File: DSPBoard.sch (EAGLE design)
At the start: 429 parts, among them IC1 AD1939WBSTZ, IC10 LM833D, IC11 LM833D, IC12 TL074D, IC2 24AA1025, IC29 TL074D, IC3 LM4040B10DBZ, IC4 LM833D, IC5 LM833D, IC6 LM833D, IC7 LM833D, IC8 LM833D, IC9 LM833D, U1 LM11173.3NOPB, U2 PEC11R-4315F-N0012, U3 PEC11R-4315F-N0012, X1 2510-, Y1 12.288MHz

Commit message: started laying out the psu
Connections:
- net GND: now also SV1.3, SV1.4, SV1.7, SV1.8
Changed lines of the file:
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@@
 <pinref part="GND9" gate="1" pin="GND"/>
 <wire x1="22.86" y1="165.1" x2="20.32" y2="165.1" width="0.1524" layer="91"/>
+<pinref part="SV1" gate="G$1" pin="4"/>
+<wire x1="22.86" y1="167.64" x2="20.32" y2="167.64" width="0.1524" layer="91"/>
+<wire x1="20.32" y1="167.64" x2="20.32" y2="165.1" width="0.1524" layer="91"/>
+<junction x="20.32" y="165.1"/>
+<pinref part="SV1" gate="G$1" pin="8"/>
+<wire x1="22.86" y1="162.56" x2="20.32" y2="162.56" width="0.1524" layer="91"/>
+<wire x1="20.32" y1="162.56" x2="20.32" y2="165.1" width="0.1524" layer="91"/>
 </segment>
 <segment>
@@
 <pinref part="GND8" gate="1" pin="GND"/>
 <wire x1="40.64" y1="165.1" x2="38.1" y2="165.1" width="0.1524" layer="91"/>
+<pinref part="SV1" gate="G$1" pin="7"/>
+<wire x1="38.1" y1="162.56" x2="40.64" y2="162.56" width="0.1524" layer="91"/>
+<wire x1="40.64" y1="162.56" x2="40.64" y2="165.1" width="0.1524" layer="91"/>
+<junction x="40.64" y="165.1"/>
+<pinref part="SV1" gate="G$1" pin="3"/>
+<wire x1="38.1" y1="167.64" x2="40.64" y2="167.64" width="0.1524" layer="91"/>
+<wire x1="40.64" y1="167.64" x2="40.64" y2="165.1" width="0.1524" layer="91"/>
 </segment>
 <segment>

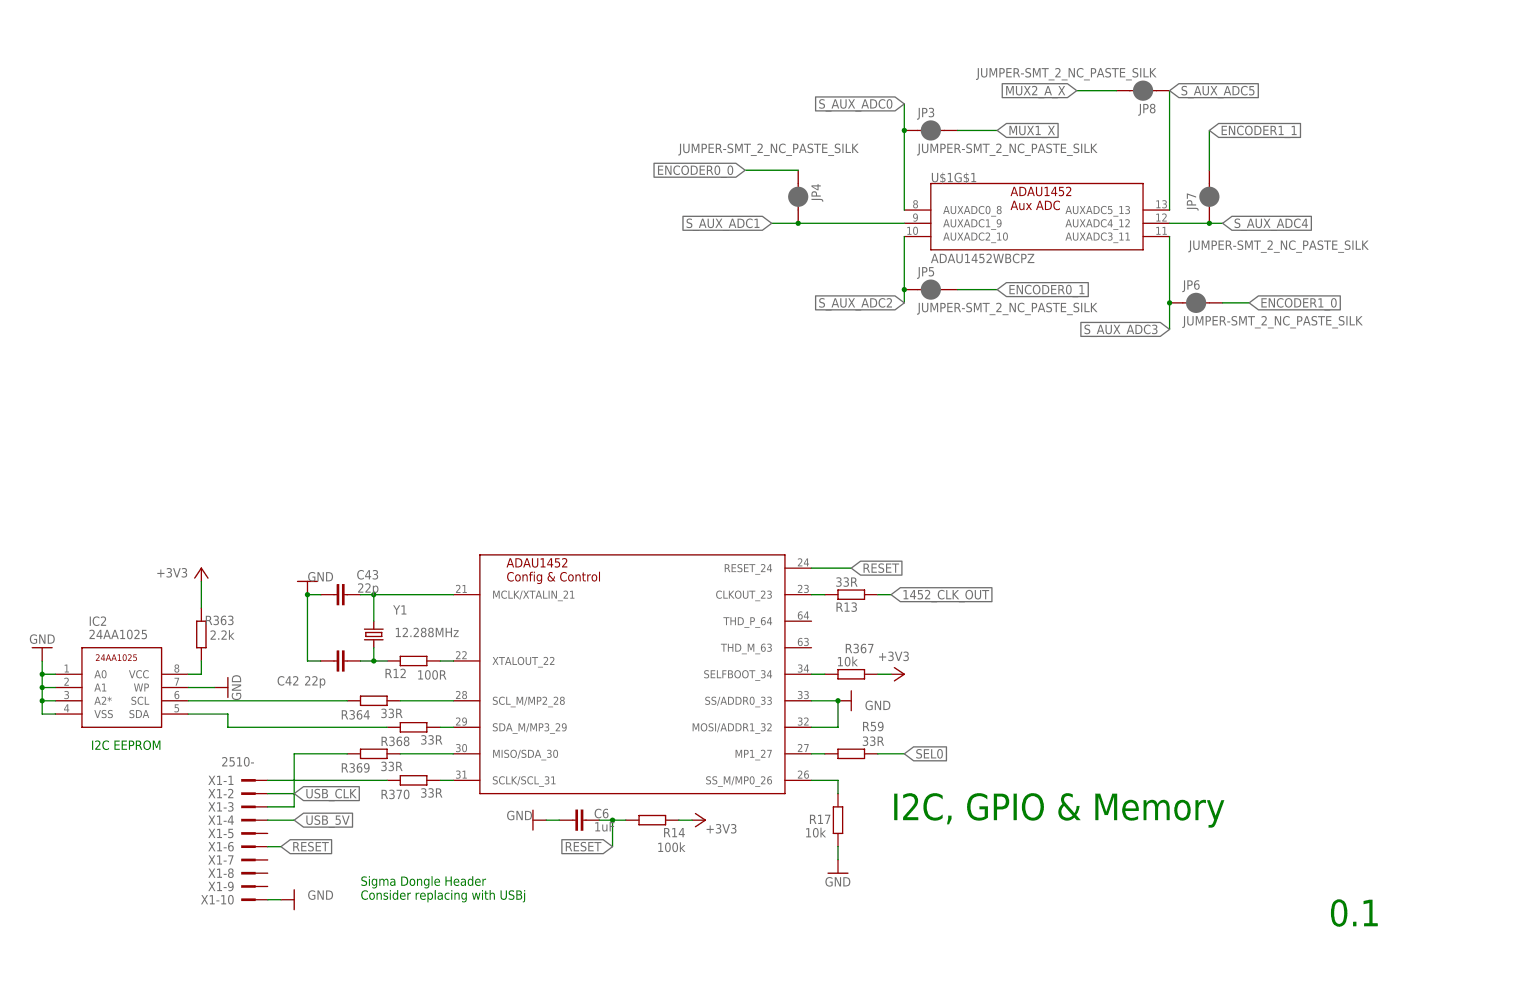
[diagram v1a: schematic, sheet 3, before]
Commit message: some layout changes, need to make daves recomended changes
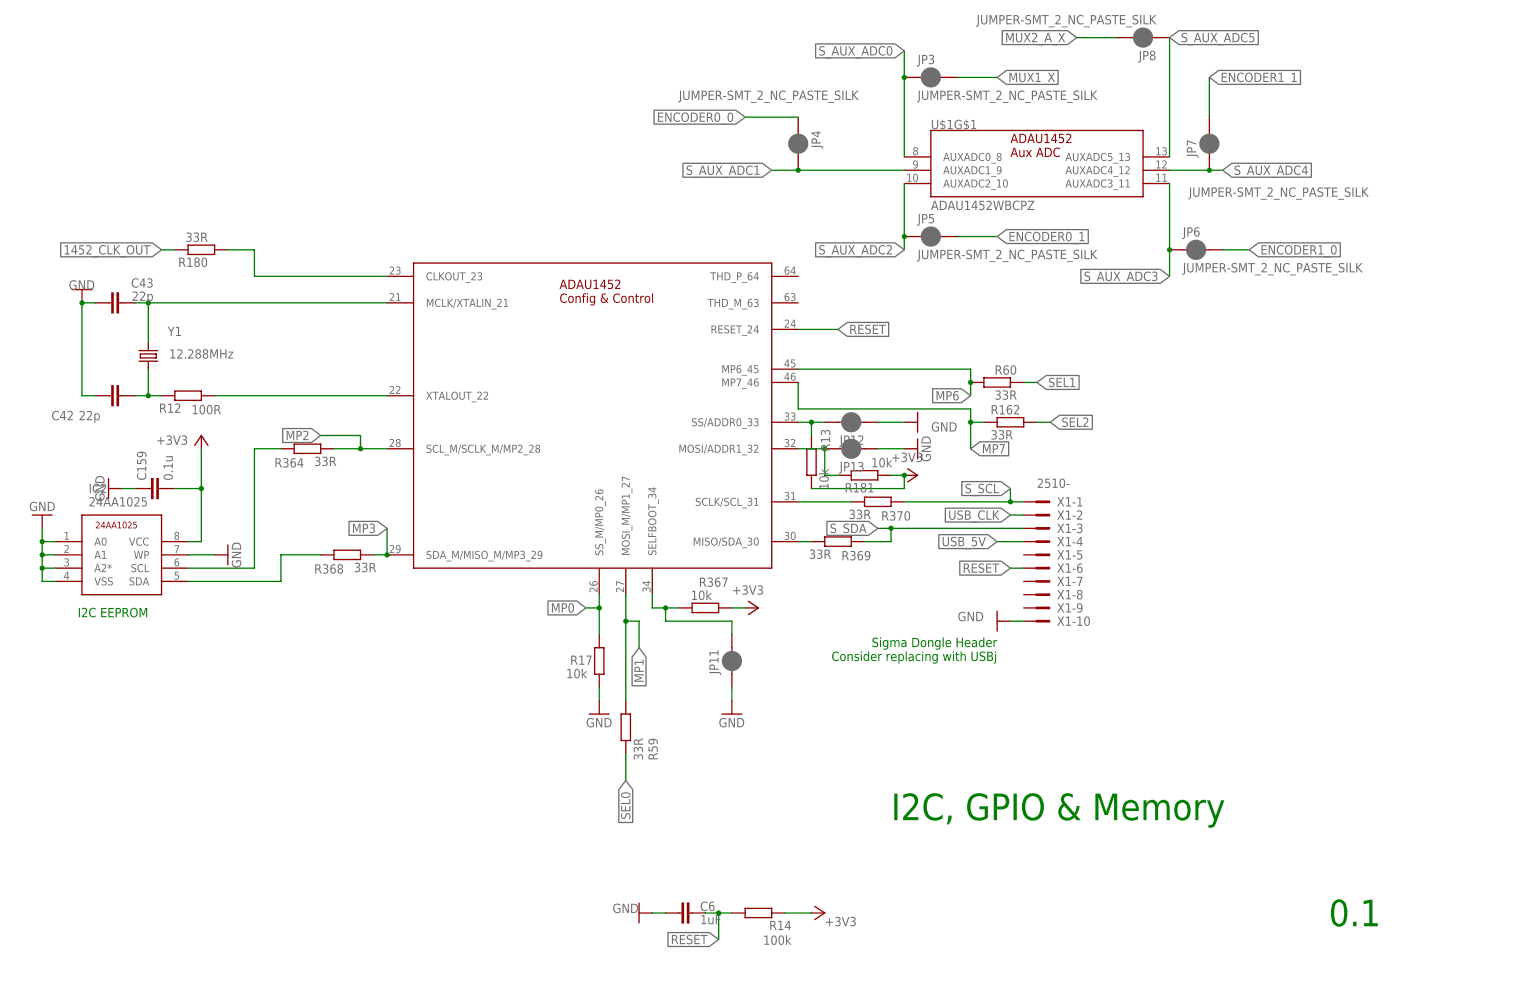
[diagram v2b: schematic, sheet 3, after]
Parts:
- removed R363: 2.2k, rcl:R-EU_R0603
- added C157, C158: 100nF, rcl:C-EUC0603
- added C159: 0.1u, rcl:C-EUC0603
- added JP11, JP12, JP13, JP14, JP15, JP16: JUMPER-SMT_2_NC_PASTE_SILK, SparkFun-Jumpers:JUMPER-SMT_2_NC_PASTE_SILK
- added R156, R157, R158, R159, R175, R176, R180: 33R, rcl:R-EU_R0603
- added R177: 240R, rcl:R-EU_R0603
- added R178: 100R, rcl:R-EU_R0603
- added R179: 75R, rcl:R-EU_R0603
- added R181: 10k, rcl:R-EU_R0603
- added SPDIF: (no value), con-lstb:MA04-1
- R13: value 33R -> 10k
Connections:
- removed net N$135: MUX2_RIPPLECOUNTERA.Q4, MUX2_RIPPLECOUNTERA.Q5, MUX2_RIPPLECOUNTERA.Q6, MUX2_RIPPLECOUNTERA.Q7, MUX2_RIPPLECOUNTERA.RES
- removed net N$162: R162.1, U$1G$5.MP7_46
- removed net N$546: R13.2, U$1G$2.CLKOUT_23
- removed net N$547: R364.1, U$1G$2.SCL_M/MP2_28
- removed net N$550: R368.1, U$1G$2.SDA_M/MP3_29
- removed net N$551: R60.2, U$1G$5.MP6_45
- removed net N$556: MUX1_RIPPLECOUNTERA.Q4, MUX1_RIPPLECOUNTERA.Q5, MUX1_RIPPLECOUNTERA.Q6, MUX1_RIPPLECOUNTERA.Q7, MUX1_RIPPLECOUNTERA.RES
- removed net N$7: IC2.VCC, R363.1
- removed net S_MP0: R174.2
- removed net S_MP1: R173.2
- removed net S_MP10: R164.2
- removed net S_MP11: R163.2
- removed net S_MP12: R161.2
- removed net S_MP13: R160.2
- removed net S_MP2: R172.2
- removed net S_MP3: R171.2
- removed net S_MP4: R170.2
- removed net S_MP5: R169.2
- removed net S_MP6: R168.2
- removed net S_MP7: R167.2
- removed net S_MP8: R166.2
- removed net S_MP9: R165.2
- new net DSP_47: JP15.1, R24.1, U$1G$5.LRCLK_OUT2/MP8_47
- new net DSP_50: JP16.1, R56.1, U$1G$5.LRCLK_OUT3/MP9_50
- new net MP0: R17.1, R174.2, U$1G$2.SS_M/MP0_26
- new net MP1: R173.2, R59.1, U$1G$2.MOSI_M/MP1_27
- new net MP10: R164.2, R8.2, U$1G$4.LRCLK_IN0/MP10_58
- new net MP11: R163.2, R27.1, U$1G$4.LRCLK_IN1/MP11_61
- new net MP12: R156.1, R161.2, U$1G$4.LRCLK_IN2/MP12_66
- new net MP13: R157.1, R160.2, U$1G$4.LRCLK_IN3/MP13_69
- new net MP2: R172.2, R364.1, U$1G$2.SCL_M/SCLK_M/MP2_28
- new net MP3: R171.2, R368.1, U$1G$2.SDA_M/MISO_M/MP3_29
- new net MP4: JP14.1, JP14.2, R170.2, R18.2, U$1G$5.LRCLK_OUT0/MP4_39
- new net MP5: R142.2, R169.2, U$1G$5.LRCLK_OUT1/MP5_42
- new net MP6: R168.2, R60.2, U$1G$2.MP6_45
- new net MP7: R162.1, R167.2, U$1G$2.MP7_46
- new net MP8: JP15.2, R166.2
- new net MP9: JP16.2, R165.2
- new net N$142: JP12.2, R13.2, U$1G$2.SS/ADDR0_33
- new net N$157: JP13.2, R181.2, U$1G$2.MOSI/ADDR1_32
- net +3V3: now also C159.2, IC2.VCC, R13.1, R181.1; no longer R363.2
- net 1452_CLK_OUT: now also R180.2; no longer R13.1
- net GND: now also C159.1, JP11.1, JP12.1, JP13.1, R178.1, R179.2, SPDIF.2, SPDIF.3; no longer U$1G$2.MOSI/ADDR1_32, U$1G$2.SS/ADDR0_33
- net N$129: now also C158.2, R177.2; no longer R18.2, U$1G$5.LRCLK_OUT0/MP4_39
- net N$130: now also R158.1, U$1G$4.SDATA_IN3_70; no longer R142.2, U$1G$5.LRCLK_OUT1/MP5_42
- net N$138: now also R177.1, R178.2, SPDIF.1; no longer R27.1, U$1G$4.LRCLK_IN1/MP11_61
- net N$141: now also R180.1, U$1G$2.CLKOUT_23; no longer R24.1, U$1G$5.LRCLK_OUT2/MP8_47
- net N$30: now also R175.2, U$1G$4.BCLK_IN2_65; no longer R17.1, U$1G$2.SS_M/MP0_26
- net N$31: now also C157.1, U$1G$6.SPDIFIN_4; no longer R59.1, U$1G$2.MP1_27
- net N$32: now also C158.1, U$1G$6.SPDIFOUT_5; no longer R370.2, X1-1.KL
- net N$33: now also R159.1, U$1G$4.BCLK_IN3_68; no longer R8.2, U$1G$4.LRCLK_IN0/MP10_58
- net N$37: now also C157.2, R179.1, SPDIF.4; no longer R369.2, X1-3.KL
- net N$39: now also R176.2, U$1G$4.SDATA_IN2_67; no longer R56.1, U$1G$5.LRCLK_OUT3/MP9_50
- net N$545: now also JP11.2
- net SDATA_IN2_BCLK: now also R175.1
- net SDATA_IN2_DATA: now also R176.1
- net SDATA_IN2_LRCLK: now also R156.2
- net SDATA_IN3_BCLK: now also R159.2
- net SDATA_IN3_DATA: now also R158.2
- net SDATA_IN3_LRCLK: now also R157.2
- net SEL1: now also MUX1_RIPPLECOUNTERA.RES
- net SEL2: now also MUX2_RIPPLECOUNTERA.RES
- net S_SCL: now also R370.2, X1-1.KL
- net S_SDA: now also R369.2, X1-3.KL
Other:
- note added: "Check that 0.1 is enough"
- moved on the sheet: C1, C2, C3, C4, C40, C41, C42, C43, C5, C6, IC2, JP3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

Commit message: double-check and confirm opamp audio gains (not CV)
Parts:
- removed C133, C49, C58, C69: 10nF, rcl:C-EUC0603
- added C160: 10uF, rcl:C-EUC0603
- added C161: 0.1uF, rcl:C-EUC0603
- added CBST: 100nF, AcceleratedDesigns_Lib:C0603C104Z3VACTUC0603C104Z3VACTU
- added CIN: 22uF, AcceleratedDesigns_Lib:C2012X5R1V226M125ACC2012X5R1V226M125AC
- added COUT: 47uF, AcceleratedDesigns_Lib:C3216X5R1E476M160ACC3216X5R1E476M160AC
- added GND: WB_GND, AcceleratedDesigns_Lib:WB_GNDWB_GND
- added IOUT: WB_CURRENT_LOAD, AcceleratedDesigns_Lib:WB_CURRENT_LOADWB_CURRENT_LOAD
- added JP17, JP18, JP19, JP20: JUMPER-SMT_2_NC_PASTE_SILK, SparkFun-Jumpers:JUMPER-SMT_2_NC_PASTE_SILK
- added L1: 4.7uH, AcceleratedDesigns_Lib:CDPH4D19FNP-4R7MCCDPH4D19FNP-4R7MC
- added R182, R183, R184, R185: 100, rcl:R-EU_R0603
- added RFBB: 10k, AcceleratedDesigns_Lib:RC0201FR-0710KLRC0201FR-0710KL
- added RFBT: 61.9k, AcceleratedDesigns_Lib:CRCW040261K9FKEDCRCW040261K9FKED
- added SV2: (no value), con-lstb:MA04-1
- added U4: TPS561201DDCR, AcceleratedDesigns_Lib:TPS561201DDCRTPS561201DDCR
- added VIN: WB_BATTERY, AcceleratedDesigns_Lib:WB_BATTERYWB_BATTERY
- C119, C121: value 22uF -> 47uF; device rcl:C-EUC0603 -> rcl:CPOL-EUD
- C122: value 0.1u -> 390pF
- C123: value 0.1u -> 5.6nF
- C137: value 0.1uF -> 100uF
- C32: value 0.1uF -> 10uF
- R135: value 562 -> 562R
- R15, R31, R49, R65: value 15k -> 18k
- R364, R368, R369, R370: value 33R -> 2k2
- R39, R46, R62, R72: value 10k -> 6k2
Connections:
- removed net DSDATA3: IC1.DSDATA3
- removed net DSDATA4: IC1.DSDATA4
- removed net N$234: D1.3, D3.3, D5.3, D7.3
- removed net N$235: D2.3, D4.3, D6.3, D8.3
- removed net N$549: IC2.SCL, R364.2
- removed net N$552: IC2.SDA, R368.2
- removed net N$553: R370.1, U$1G$2.SCLK/SCL_31
- removed net N$554: R369.1, U$1G$2.MISO/SDA_30
- new net 0: CIN.2@2, COUT.2@2, GND.1@1, IOUT.-@2, RFBB.2@2, U4.GND@1, VIN.-@2
- new net 1: CIN.1@1, U4.EN@5, U4.VIN@3, VIN.+@1
- new net 2: CBST.1@1, L1.1@1, U4.SW@2
- new net 3: RFBB.1@1, RFBT.2@2, U4.VFB@4
- new net 4: COUT.1@1, IOUT.+@1, L1.2@2, RFBT.1@1
- new net 5: CBST.2@2, U4.VBST@6
- new net N$135: IC1.!CLATCH, JP20.1, SV2.1
- new net N$158: IC1.CCLK, JP19.1, SV2.2
- new net N$159: IC1.COUT, JP18.1, SV2.3
- new net N$160: R182.2, R39.1
- new net N$161: R185.2, R46.1
- new net N$162: R183.2, R62.1
- new net N$163: R184.2, R72.1
- new net N$7: IC1.CIN, JP17.1, SV2.4
- net +3V3: now also C160.2, C161.2, R364.2, R368.1, R369.1, R370.1
- net AIN0+: now also D2.3
- net AIN0-: now also D1.3
- net AIN1+: now also D4.3
- net AIN1-: now also D3.3
- net AIN2+: now also D7.3
- net AIN2-: now also D8.3
- net AIN3+: now also D6.3
- net AIN3-: now also D5.3
- net ASDATA2: no longer IC1.ASDATA2
- net DSDATA2: no longer IC1.DSDATA2
- net FILTR: now also C121.+; no longer C121.1
- net GND: now also C119.-, C121.-, C160.1, C161.1, JP17.2, JP18.2, JP19.2, JP20.2; no longer C119.2, C121.2, IC1.!CLATCH, IC1.CCLK, IC1.CIN, IC1.COUT
- net MP2: now also IC2.SCL
- net MP3: now also IC2.SDA, R368.2; no longer R368.1
- net N$10: no longer C49.1
- net N$18: now also R182.1; no longer R39.1
- net N$36: now also R185.1; no longer R46.1
- net N$38: no longer C58.2
- net N$40: no longer C58.1
- net N$47: now also R183.1; no longer R62.1
- net N$48: no longer C69.2
- net N$49: no longer C69.1
- net N$56: now also R184.1; no longer R72.1
- net N$57: no longer C133.2
- net N$58: no longer C133.1
- net N$75: now also C119.+; no longer C119.1
- net N$9: no longer C49.2
- net S_SCL: now also U$1G$2.SCLK/SCL_31
- net S_SDA: now also U$1G$2.MISO/SDA_30
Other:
- note removed: "Check that 0.1 is enough"

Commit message: Chekcing and some bug fixes complete, plus psu layout touchup
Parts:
- removed C156: 100n, rcl:C-EUC0603
- removed CBST: 100nF, AcceleratedDesigns_Lib:C0603C104Z3VACTUC0603C104Z3VACTU
- removed CIN: 22uF, AcceleratedDesigns_Lib:C2012X5R1V226M125ACC2012X5R1V226M125AC
- removed COUT: 47uF, AcceleratedDesigns_Lib:C3216X5R1E476M160ACC3216X5R1E476M160AC
- removed GND: WB_GND, AcceleratedDesigns_Lib:WB_GNDWB_GND
- removed IOUT: WB_CURRENT_LOAD, AcceleratedDesigns_Lib:WB_CURRENT_LOADWB_CURRENT_LOAD
- removed L1: 4.7uH, AcceleratedDesigns_Lib:CDPH4D19FNP-4R7MCCDPH4D19FNP-4R7MC
- removed MUX1_RIPPLECOUNTER, MUX2_RIPPLECOUNTER: 4024D, 40xx:4024D
- removed RFBB: 10k, AcceleratedDesigns_Lib:RC0201FR-0710KLRC0201FR-0710KL
- removed RFBT: 61.9k, AcceleratedDesigns_Lib:CRCW040261K9FKEDCRCW040261K9FKED
- removed U4: TPS561201DDCR, AcceleratedDesigns_Lib:TPS561201DDCRTPS561201DDCR
- removed VIN: WB_BATTERY, AcceleratedDesigns_Lib:WB_BATTERYWB_BATTERY
- added IC13: 4520D, 45xx:4520D
- C128, C129, C130, C131, C146, C147, C150, C151: value 0.1u -> 1n
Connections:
- removed net 0: CIN.2@2, COUT.2@2, GND.1@1, IOUT.-@2, RFBB.2@2, U4.GND@1, VIN.-@2
- removed net 1: CIN.1@1, U4.EN@5, U4.VIN@3, VIN.+@1
- removed net 2: CBST.1@1, L1.1@1, U4.SW@2
- removed net 3: RFBB.1@1, RFBT.2@2, U4.VFB@4
- removed net 4: COUT.1@1, IOUT.+@1, L1.2@2, RFBT.1@1
- removed net 5: CBST.2@2, U4.VBST@6
- net +5V: now also IC13P.VDD; no longer C156.1, MUX1_RIPPLECOUNTERP.VDD, MUX2_RIPPLECOUNTERP.VDD
- net GND: now also IC12B.+IN, IC12D.+IN, IC13P.VSS, IC29B.+IN, IC29D.+IN; no longer C156.2, IC12B.-IN, IC12D.-IN, IC29B.-IN, IC29D.-IN, MUX1_RIPPLECOUNTERP.VSS, MUX2_RIPPLECOUNTERP.VSS
- net MUX1_A: now also IC13A.Q0; no longer MUX1_RIPPLECOUNTERA.Q1
- net MUX1_B: now also IC13A.Q1; no longer MUX1_RIPPLECOUNTERA.Q2
- net MUX1_C: now also IC13A.Q2; no longer MUX1_RIPPLECOUNTERA.Q3
- net MUX2_A_A: now also IC13B.Q0; no longer MUX2_RIPPLECOUNTERA.Q1
- net MUX2_A_B: now also IC13B.Q1; no longer MUX2_RIPPLECOUNTERA.Q2
- net MUX2_A_C: now also IC13B.Q2; no longer MUX2_RIPPLECOUNTERA.Q3
- net N$116: now also IC12B.-IN; no longer IC12B.+IN
- net N$122: now also IC12D.-IN; no longer IC12D.+IN
- net N$540: now also IC29B.-IN; no longer IC29B.+IN
- net N$543: now also IC29D.-IN; no longer IC29D.+IN
- net SDATA_OUT2_LRCLK: now also IC13A.CLK, IC13B.CLK; no longer MUX1_RIPPLECOUNTERA.CLK, MUX2_RIPPLECOUNTERA.CLK
- net SEL1: now also IC13A.EN, IC13B.EN; no longer MUX1_RIPPLECOUNTERA.RES
- net SEL2: now also IC13A.RES, IC13B.RES; no longer MUX2_RIPPLECOUNTERA.RES

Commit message: grinding through
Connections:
- net ASDATA2: now also IC1.ASDATA2
- net DSDATA2: now also IC1.DSDATA2
- net ENCODER0_0: now also JP4.2; no longer JP4.1
- net S_AUX_ADC1: now also JP4.1; no longer JP4.2
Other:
- moved on the sheet: JP4
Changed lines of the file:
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@@
 <wire x1="198.12" y1="121.92" x2="198.12" y2="116.84" width="0.1524" layer="91"/>
 <junction x="198.12" y="116.84"/>
+<label x="205.74" y="121.92" size="1.778" layer="95" rot="R180"/>
 </segment>
 <segment>
@@
 <wire x1="160.02" y1="157.48" x2="144.78" y2="157.48" width="0.1524" layer="91"/>
 <junction x="144.78" y="157.48"/>
+<label x="190.5" y="139.7" size="1.778" layer="95" rot="R180"/>
 </segment>
 </net>
@@
 <attribute name="VALUE" x="172.72" y="165.1" size="1.778" layer="96" font="vector" align="top-left"/>
 </instance>
-<instance part="JP4" gate="G$1" x="149.86" y="154.94" smashed="yes" rot="R270">
-<attribute name="NAME" x="152.4" y="157.48" size="1.778" layer="95" font="vector" rot="R270"/>
-<attribute name="VALUE" x="127" y="165.1" size="1.778" layer="96" font="vector" align="top-left"/>
+<instance part="JP4" gate="G$1" x="152.4" y="162.56" smashed="yes" rot="R90">
+<attribute name="NAME" x="149.86" y="160.02" size="1.778" layer="95" font="vector" rot="R90"/>
+<attribute name="VALUE" x="175.26" y="152.4" size="1.778" layer="96" font="vector" rot="R180" align="top-left"/>
 </instance>
 <instance part="JP5" gate="G$1" x="175.26" y="137.16" smashed="yes">
@@
 <net name="S_AUX_ADC1" class="0">
 <segment>
+<label x="144.78" y="149.86" size="1.778" layer="95" rot="R180" xref="yes"/>
 <pinref part="U$1" gate="G$1" pin="AUXADC1_9"/>
-<wire x1="170.18" y1="149.86" x2="149.86" y2="149.86" width="0.1524" layer="91"/>
-<label x="144.78" y="149.86" size="1.778" layer="95" rot="R180" xref="yes"/>
-<pinref part="JP4" gate="G$1" pin="2"/>
-<wire x1="149.86" y1="149.86" x2="144.78" y2="149.86" width="0.1524" layer="91"/>
-<junction x="149.86" y="149.86"/>
+<wire x1="170.18" y1="149.86" x2="152.4" y2="149.86" width="0.1524" layer="91"/>
+<pinref part="JP4" gate="G$1" pin="1"/>
+<wire x1="152.4" y1="149.86" x2="144.78" y2="149.86" width="0.1524" layer="91"/>
+<wire x1="152.4" y1="157.48" x2="152.4" y2="149.86" width="0.1524" layer="91"/>
+<junction x="152.4" y="149.86"/>
 </segment>
 </net>
@@
 <net name="ENCODER0_0" class="0">
 <segment>
-<pinref part="JP4" gate="G$1" pin="1"/>
-<wire x1="149.86" y1="160.02" x2="139.7" y2="160.02" width="0.1524" layer="91"/>
-<label x="139.7" y="160.02" size="1.778" layer="95" rot="R180" xref="yes"/>
+<label x="119.38" y="162.56" size="1.778" layer="95" rot="R180" xref="yes"/>
+<pinref part="JP4" gate="G$1" pin="2"/>
+<wire x1="119.38" y1="162.56" x2="119.38" y2="167.64" width="0.1524" layer="91"/>
+<wire x1="119.38" y1="167.64" x2="152.4" y2="167.64" width="0.1524" layer="91"/>
 </segment>
 </net>
@@
 </instance>
 <instance part="R27" gate="G$1" x="162.56" y="152.4" smashed="yes" rot="R180">
-<attribute name="NAME" x="166.37" y="150.9014" size="1.778" layer="95" rot="R180"/>
+<attribute name="NAME" x="161.29" y="150.9014" size="1.778" layer="95" rot="R180"/>
 <attribute name="VALUE" x="166.37" y="155.702" size="1.778" layer="96" rot="R180"/>
 </instance>
@@
 <label x="127" y="60.96" size="1.778" layer="95" rot="R180" xref="yes"/>
 </segment>
+<segment>
+<pinref part="IC1" gate="G$1" pin="DSDATA2"/>
+<wire x1="60.96" y1="73.66" x2="60.96" y2="60.96" width="0.1524" layer="91"/>
+<label x="60.96" y="60.96" size="1.778" layer="95" rot="R180" xref="yes"/>
+</segment>
 </net>
 <net name="DSDATA1" class="0">
@@
 <label x="154.94" y="147.32" size="1.778" layer="95" rot="R180" xref="yes"/>
 </segment>
-</net>
+<segment>
+<pinref part="IC1" gate="G$1" pin="ASDATA2"/>
+<wire x1="78.74" y1="73.66" x2="78.74" y2="50.8" width="0.1524" layer="91"/>
+<label x="78.74" y="50.8" size="1.778" layer="95" rot="R180" xref="yes"/>
+</segment>
+</net>

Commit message: continuing to layout
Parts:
- removed SV2: (no value), con-lstb:MA04-1
- added TP1, TP2, TP3, TP4: TESTPAD_TPSQTP16R, BeagleBone_Blue_R3:TESTPAD_TPSQTP16R
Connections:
- net +3V3: no longer D1.1, D2.2, D3.1, D4.2, D5.1, D6.2, D7.1, D8.2
- net 3V3A: now also D1.1, D2.2, D3.1, D4.2, D5.1, D6.2, D7.1, D8.2
- net N$135: now also TP4.TP; no longer SV2.1
- net N$158: now also TP3.TP; no longer SV2.2
- net N$159: now also TP2.TP; no longer SV2.3
- net N$7: now also TP1.TP; no longer SV2.4
